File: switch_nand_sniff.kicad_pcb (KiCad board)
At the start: 2 copper layers, 20.8 x 28.1 mm, 18 parts, among them P1 CONN_02X15, P2 CONN_02X15, P3 CONN_01X08, P4 CONN_01X08

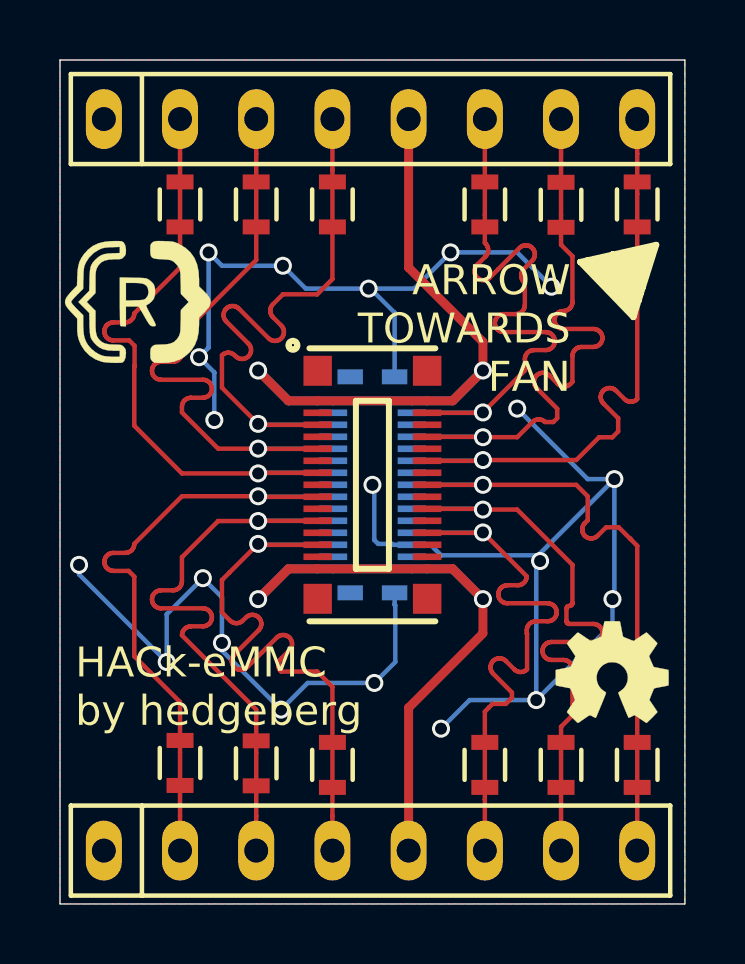
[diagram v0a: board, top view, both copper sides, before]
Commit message: Updated main board for rev3. *Improved manufacturability for larger scale production. *Added pin labels on reverse side for easy mapping during sniffing.
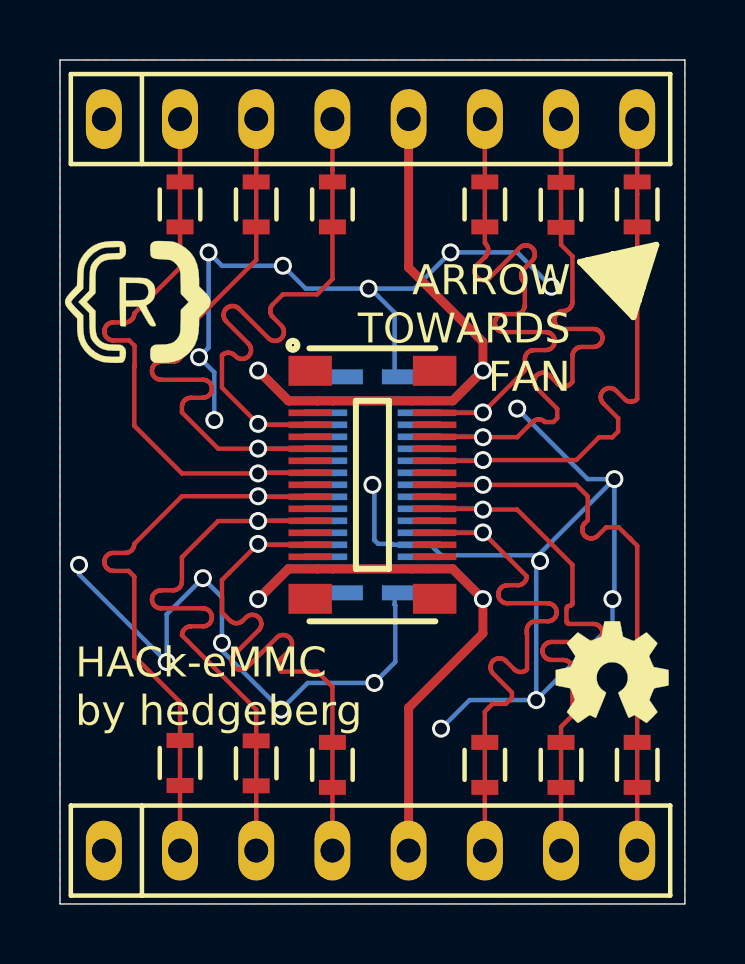
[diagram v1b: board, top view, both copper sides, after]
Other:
- board text added: "1V8"
- board text added: "3V3"
- board text added: "???"
- board text added: "CLK"
- board text added: "CMD"
- board text added: "D0"
- board text added: "D1"
- board text added: "D2"
- board text added: "D3"
- board text added: "D4"
- board text added: "D5"
- board text added: "D6"
- board text added: "D7"
- board text added: "GND"
- board text added: "RST"
